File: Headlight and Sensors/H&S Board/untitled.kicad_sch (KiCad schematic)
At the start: 15 parts, among them U7 MCP6286T-E/OT, U8 MCP6286T-E/OT, U9 MCP6286T-E/OT

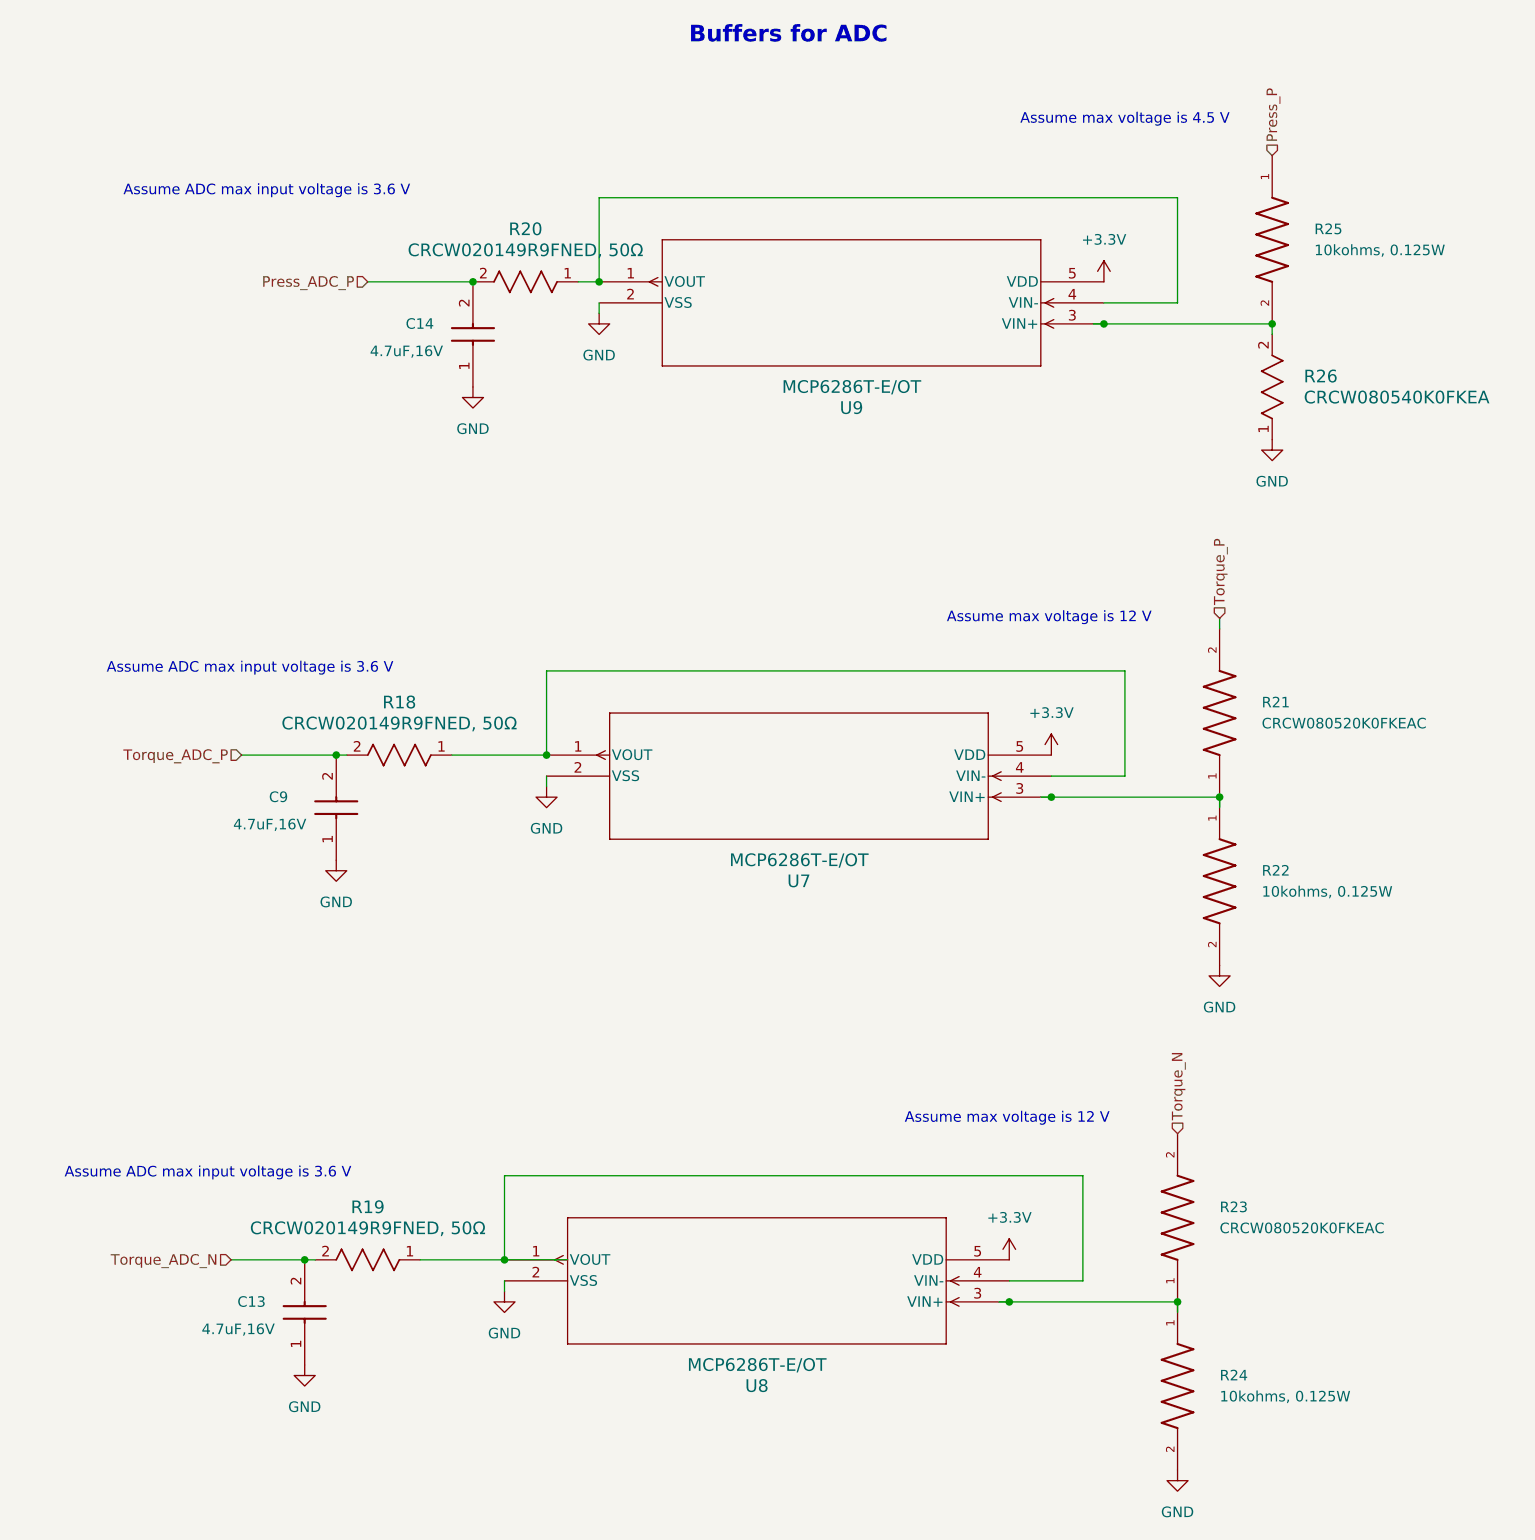
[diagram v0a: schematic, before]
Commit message: fixed resistance values
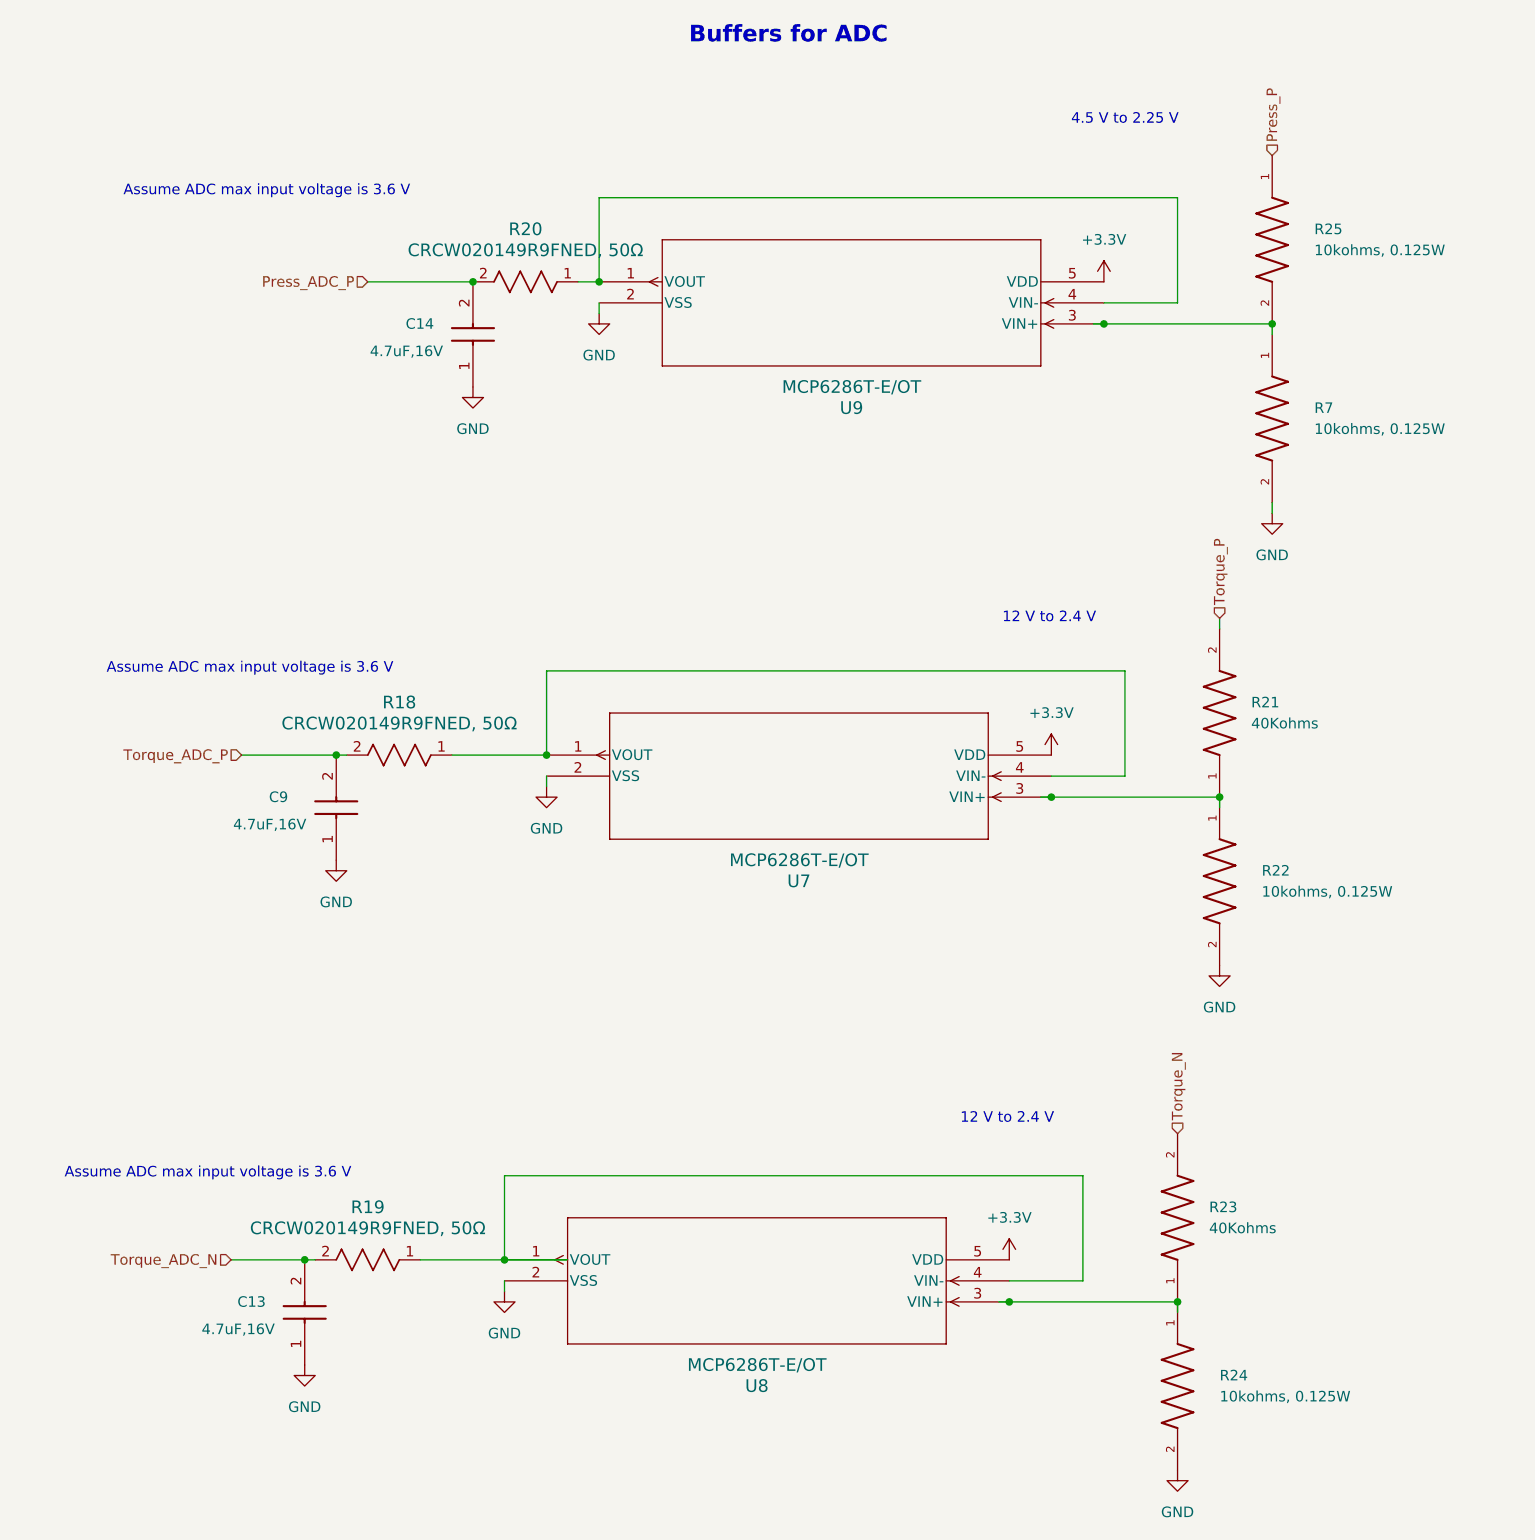
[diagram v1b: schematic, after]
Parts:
- removed R26: CRCW080540K0FKEA, SMV_Passives:0805RESC2012X60N, symbol SMV_Custom:CRCW080540K0FKEA
- added R7: 10kohms, 0.125W, SMV_Passives:0805RESC2012X60N, symbol SMV_Custom:CRCW080510K0FKEAC
- R21, R23: value CRCW080520K0FKEAC -> 40Kohms
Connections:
- net GND: now also R7.2
- net at R25.2, U9.3 (VIN+): now also R7.1
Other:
- note added: "12 V to 2.4 V"
- note added: "4.5 V to 2.25 V"
- note removed: "Assume max voltage is 12 V"
- note removed: "Assume max voltage is 4.5 V"
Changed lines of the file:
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@@
+	(wire
+		(pts
+			(xy 162.56 73.66) (xy 162.56 72.39)
+		)
+		(stroke
+			(width 0)
+			(type default)
+		)
+	)
 	(wire
 		(pts
@@
 		)
 	)
-	(text "Assume max voltage is 12 V\n"
+	(text "12 V to 2.4 V\n"
 		(exclude_from_sim no)
 		(at 135.636 86.36 0)
@@
 		)
 	)
-	(text "Assume max voltage is 12 V\n"
+	(text "12 V to 2.4 V"
 		(exclude_from_sim no)
 		(at 130.556 146.812 0)
@@
 		)
 	)
-	(text "Assume max voltage is 4.5 V\n"
+	(text "4.5 V to 2.25 V"
 		(exclude_from_sim no)
 		(at 144.78 26.162 0)
@@
 	)
 	(symbol
-		(lib_id "SMV_Custom:CRCW080540K0FKEA")
-		(at 162.56 64.77 90)
-		(unit 1)
-		(exclude_from_sim no)
-		(in_bom yes)
-		(on_board yes)
-		(dnp no)
-		(fields_autoplaced yes)
-		(property "Reference" "R26"
-			(at 166.37 57.1499 90)
-			(effects
-				(font
-					(size 1.524 1.524)
-				)
-				(justify right)
-			)
-		)
-		(property "Value" "CRCW080540K0FKEA"
-			(at 166.37 59.6899 90)
-			(effects
-				(font
-					(size 1.524 1.524)
-				)
-				(justify right)
-			)
-		)
-		(property "Footprint" "SMV_Passives:0805RESC2012X60N"
-			(at 162.56 64.77 0)
-			(effects
-				(font
-					(size 1.27 1.27)
-					(italic yes)
-				)
-				(hide yes)
-			)
-		)
-		(property "Datasheet" "CRCW080540K0FKEA"
-			(at 162.56 64.77 0)
-			(effects
-				(font
-					(size 1.27 1.27)
-					(italic yes)
-				)
-				(hide yes)
-			)
-		)
-		(property "Description" ""
-			(at 162.56 64.77 0)
-			(effects
-				(font
-					(size 1.27 1.27)
-				)
-				(hide yes)
-			)
-		)
-		(pin "2"
-		)
-		(pin "1"
-		)
-		(instances
-			(project "H&S Board"
-				(path "/cdf86217-7949-4457-8f19-2e0a76b22e93/4f2484e1-7207-412d-9e54-f6a8af7276f8"
-					(reference "R26")
-					(unit 1)
-				)
-			)
-		)
-	)
-	(symbol
 		(lib_id "power:GND")
 		(at 156.21 128.27 0)
@@
 		(fields_autoplaced yes)
 		(property "Reference" "R23"
-			(at 156.21 157.4799 90)
+			(at 154.94 157.4799 90)
 			(effects
 				(font
@@
 			)
 		)
-		(property "Value" "CRCW080520K0FKEAC"
-			(at 156.21 160.0199 90)
+		(property "Value" "40Kohms"
+			(at 154.94 160.0199 90)
 			(effects
 				(font
@@
 	)
 	(symbol
+		(lib_id "SMV_Custom:CRCW080510K0FKEAC")
+		(at 162.56 62.23 270)
+		(unit 1)
+		(exclude_from_sim no)
+		(in_bom yes)
+		(on_board yes)
+		(dnp no)
+		(fields_autoplaced yes)
+		(property "Reference" "R7"
+			(at 167.64 60.9599 90)
+			(effects
+				(font
+					(size 1.27 1.27)
+				)
+				(justify left)
+			)
+		)
+		(property "Value" "10kohms, 0.125W"
+			(at 167.64 63.4999 90)
+			(effects
+				(font
+					(size 1.27 1.27)
+				)
+				(justify left)
+			)
+		)
+		(property "Footprint" "SMV_Passives:0805RESC2012X60N"
+			(at 162.56 62.23 0)
+			(effects
+				(font
+					(size 1.27 1.27)
+				)
+				(justify bottom)
+				(hide yes)
+			)
+		)
+		(property "Datasheet" ""
+			(at 162.56 62.23 0)
+			(effects
+				(font
+					(size 1.27 1.27)
+				)
+				(hide yes)
+			)
+		)
+		(property "Description" ""
+			(at 162.56 62.23 0)
+			(effects
+				(font
+					(size 1.27 1.27)
+				)
+				(hide yes)
+			)
+		)
+		(property "MF" "Vishay Dale"
+			(at 162.56 62.23 0)
+			(effects
+				(font
+					(size 1.27 1.27)
+				)
+				(justify bottom)
+				(hide yes)
+			)
+		)
+		(property "Description_1" "\n                        \n                            10 kOhms ±1% 0.125W, 1/8W Chip Resistor 0805 (2012 Metric) - Thick Film\n                        \n"
+			(at 162.56 62.23 0)
+			(effects
+				(font
+					(size 1.27 1.27)
+				)
+				(justify bottom)
+				(hide yes)
+			)
+		)
+		(property "Package" "2012 Vishay"
+			(at 162.56 62.23 0)
+			(effects
+				(font
+					(size 1.27 1.27)
+				)
+				(justify bottom)
+				(hide yes)
+			)
+		)
+		(property "Price" "None"
+			(at 162.56 62.23 0)
+			(effects
+				(font
+					(size 1.27 1.27)
+				)
+				(justify bottom)
+				(hide yes)
+			)
+		)
+		(property "SnapEDA_Link" "https://www.snapeda.com/parts/CRCW080510K0FKEAC/Vishay+Dale/view-part/?ref=snap"
+			(at 162.56 62.23 0)
+			(effects
+				(font
+					(size 1.27 1.27)
+				)
+				(justify bottom)
+				(hide yes)
+			)
+		)
+		(property "MP" "CRCW080510K0FKEAC"
+			(at 162.56 62.23 0)
+			(effects
+				(font
+					(size 1.27 1.27)
+				)
+				(justify bottom)
+				(hide yes)
+			)
+		)
+		(property "Availability" "In Stock"
+			(at 162.56 62.23 0)
+			(effects
+				(font
+					(size 1.27 1.27)
+				)
+				(justify bottom)
+				(hide yes)
+			)
+		)
+		(property "Check_prices" "https://www.snapeda.com/parts/CRCW080510K0FKEAC/Vishay+Dale/view-part/?ref=eda"
+			(at 162.56 62.23 0)
+			(effects
+				(font
+					(size 1.27 1.27)
+				)
+				(justify bottom)
+				(hide yes)
+			)
+		)
+		(pin "2"
+		)
+		(pin "1"
+		)
+		(instances
+			(project "H&S Board"
+				(path "/cdf86217-7949-4457-8f19-2e0a76b22e93/4f2484e1-7207-412d-9e54-f6a8af7276f8"
+					(reference "R7")
+					(unit 1)
+				)
+			)
+		)
+	)
+	(symbol
 		(lib_id "SMV_Custom:CRCW020149R9FNED")
 		(at 66.04 45.72 0)
@@
 	(symbol
 		(lib_id "power:GND")
-		(at 162.56 64.77 0)
+		(at 162.56 73.66 0)
 		(unit 1)
 		(exclude_from_sim no)
@@
 		(dnp no)
 		(property "Reference" "#PWR063"
-			(at 162.56 71.12 0)
+			(at 162.56 80.01 0)
 			(effects
 				(font
@@
 		)
 		(property "Value" "GND"
-			(at 162.56 69.85 0)
+			(at 162.56 78.74 0)
 			(effects
 				(font
@@
 		)
 		(property "Footprint" ""
-			(at 162.56 64.77 0)
+			(at 162.56 73.66 0)
 			(effects
 				(font
@@
 		)
 		(property "Datasheet" ""
-			(at 162.56 64.77 0)
+			(at 162.56 73.66 0)
 			(effects
 				(font
@@
 		)
 		(property "Description" "Power symbol creates a global label with name \"GND\" , ground"
-			(at 162.56 64.77 0)
+			(at 162.56 73.66 0)
 			(effects
 				(font
@@
 		(fields_autoplaced yes)
 		(property "Reference" "R21"
-			(at 161.29 96.5199 90)
+			(at 160.02 96.5199 90)
 			(effects
 				(font
@@
 			)
 		)
-		(property "Value" "CRCW080520K0FKEAC"
-			(at 161.29 99.0599 90)
-			(effects
-				(font
+		(property "Value" "40Kohms"
+			(at 160.02 99.0599 90)
+			(effects
+				(font

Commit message: PCB rough draft
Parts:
- added C5, C7, C8: 0.1 uF, SMV_Passives:Cap0805, symbol SMV_Custom:C0805C475K4RACTU
- C13, C14, C9: value 4.7uF,16V -> 4.7nF,16V
- R21: value 40Kohms -> 10Kohms
- R25: value 10kohms, 0.125W -> 40kohms
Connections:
- net +3.3V: now also C5.1, C7.1, C8.1
- net GND: now also C5.2, C7.2, C8.2
- net Press_ADC_P: now also C9.2, R18.2; no longer C14.2, R20.2
- net Press_P: now also R21.2; no longer R25.1
- net Torque_ADC_N: now also C14.2, R20.2; no longer C13.2, R19.2
- net Torque_ADC_P: now also C13.2, R19.2; no longer C9.2, R18.2
- net Torque_N: now also R25.1; no longer R23.2
- net Torque_P: now also R23.2; no longer R21.2
